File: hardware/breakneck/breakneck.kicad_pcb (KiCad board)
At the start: 2 copper layers, 53.3 x 64 mm, 82 parts, among them J1 CONN_EAST, J10 CONN_WEST, J2 GS2, J3 CONN_01X02, J4 GS3, J5 USB_C_Receptacle, J6 GS3, J7 CONN_OLED, J8 CONN_SOUTH, J9 CONN_JTAG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

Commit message: Flush connections from first batch of design rule check results.
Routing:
- net GND: track 43.6 -> 128.6 mm, vias 3 -> 16
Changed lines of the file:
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@@
   (general
     (links 242)
-    (no_connects 108)
-    (area 99.924999 63.924999 153.415001 128.075001)
+    (no_connects 94)
+    (area 87.650001 56.8 244.600001 146.625)
     (thickness 1.6)
     (drawings 59)
-    (tracks 478)
+    (tracks 541)
     (zones 0)
     (modules 82)
@@
   (segment (start 134.95 108.2) (end 137.1 108.2) (width 0.1524) (layer F.Cu) (net 1))
   (segment (start 133.5 106.75) (end 134.95 108.2) (width 0.1524) (layer F.Cu) (net 1))
+  (segment (start 121.4 112) (end 121.4 111.4) (width 0.1524) (layer F.Cu) (net 2))
+  (segment (start 121.4 111.4) (end 121 111) (width 0.1524) (layer F.Cu) (net 2))
+  (via (at 121 111) (size 0.6858) (drill 0.3302) (layers F.Cu B.Cu) (net 2))
+  (segment (start 121.4 112) (end 121.4 113.84) (width 0.1524) (layer F.Cu) (net 2))
+  (segment (start 121.4 113.84) (end 125.4 117.84) (width 0.1524) (layer F.Cu) (net 2))
+  (segment (start 125.4 117.84) (end 126.56 117.84) (width 0.1524) (layer F.Cu) (net 2))
+  (segment (start 126.56 117.84) (end 130 114.4) (width 0.1524) (layer F.Cu) (net 2))
+  (segment (start 132 116.5) (end 132 116.4) (width 0.1524) (layer F.Cu) (net 2))
+  (segment (start 132 116.4) (end 130 114.4) (width 0.1524) (layer F.Cu) (net 2))
+  (segment (start 142.2 103.9) (end 148.07 103.9) (width 0.1524) (layer F.Cu) (net 2))
+  (via (at 142.2 103.9) (size 0.6858) (drill 0.3302) (layers F.Cu B.Cu) (net 2))
+  (segment (start 140.11 103.9) (end 142.2 103.9) (width 0.1524) (layer B.Cu) (net 2))
+  (segment (start 148.065 103.895) (end 148.07 103.9) (width 0.1524) (layer F.Cu) (net 2))
+  (via (at 148.07 103.9) (size 0.6858) (drill 0.3302) (layers F.Cu B.Cu) (net 2))
+  (segment (start 148.065 103.895) (end 148.07 102.75) (width 0.1524) (layer F.Cu) (net 2) (status 20))
+  (segment (start 145.7 103.14) (end 147.68 103.14) (width 0.1524) (layer F.Cu) (net 2) (status 20))
+  (segment (start 140.11 103.9) (end 140.11 102.61) (width 0.1524) (layer B.Cu) (net 2))
+  (via (at 136 100) (size 0.6858) (drill 0.3302) (layers F.Cu B.Cu) (net 2))
+  (segment (start 136 101.5) (end 136 100) (width 0.1524) (layer F.Cu) (net 2))
+  (segment (start 140.11 103.9) (end 140.11 102.75) (width 0.1524) (layer F.Cu) (net 2) (status 20))
+  (via (at 140.11 103.9) (size 0.6858) (drill 0.3302) (layers F.Cu B.Cu) (net 2))
+  (segment (start 137.5 100) (end 136 100) (width 0.1524) (layer B.Cu) (net 2))
+  (segment (start 140.11 102.61) (end 137.5 100) (width 0.1524) (layer B.Cu) (net 2))
+  (segment (start 137.7 106.25) (end 137.7 107.2) (width 0.1524) (layer F.Cu) (net 2))
+  (via (at 142.25 109) (size 0.6858) (drill 0.3302) (layers F.Cu B.Cu) (net 2))
+  (segment (start 140.75 109) (end 142.25 109) (width 0.1524) (layer B.Cu) (net 2))
+  (via (at 140.75 109) (size 0.6858) (drill 0.3302) (layers F.Cu B.Cu) (net 2))
+  (segment (start 139.5 109) (end 140.75 109) (width 0.1524) (layer F.Cu) (net 2))
+  (segment (start 137.7 107.2) (end 139.5 109) (width 0.1524) (layer F.Cu) (net 2))
+  (segment (start 135.3 110.25) (end 135.3 110.2) (width 0.1524) (layer F.Cu) (net 2))
+  (segment (start 135.3 110.2) (end 136.5 109) (width 0.1524) (layer F.Cu) (net 2))
+  (segment (start 136.5 107.5) (end 137.7 106.3) (width 0.1524) (layer F.Cu) (net 2))
+  (via (at 136.5 107.5) (size 0.6858) (drill 0.3302) (layers F.Cu B.Cu) (net 2))
+  (segment (start 136.5 109) (end 136.5 107.5) (width 0.1524) (layer B.Cu) (net 2))
+  (via (at 136.5 109) (size 0.6858) (drill 0.3302) (layers F.Cu B.Cu) (net 2))
+  (segment (start 137.7 106.3) (end 137.7 106.25) (width 0.1524) (layer F.Cu) (net 2))
+  (segment (start 135.5 112.5) (end 135.5 110.45) (width 0.1524) (layer F.Cu) (net 2))
+  (segment (start 135.5 110.45) (end 135.3 110.25) (width 0.1524) (layer F.Cu) (net 2))
+  (segment (start 137.5 104) (end 137.5 106.05) (width 0.1524) (layer F.Cu) (net 2))
+  (segment (start 137.5 106.05) (end 137.7 106.25) (width 0.1524) (layer F.Cu) (net 2))
+  (segment (start 147.68 103.14) (end 148.07 102.75) (width 0.1524) (layer F.Cu) (net 2) (status 30))
+  (segment (start 140.2 118.88) (end 139.28 118.88) (width 0.1524) (layer F.Cu) (net 2))
+  (segment (start 139.28 118.88) (end 139.07 119.09) (width 0.1524) (layer F.Cu) (net 2))
+  (segment (start 132.42 112.5) (end 132.42 111.25) (width 0.1524) (layer F.Cu) (net 2))
+  (via (at 132.42 111.25) (size 0.6858) (drill 0.3302) (layers F.Cu B.Cu) (net 2))
+  (segment (start 129.92 110.7) (end 129.92 111.5) (width 0.1524) (layer F.Cu) (net 2))
+  (via (at 128.9 112) (size 0.6858) (drill 0.3302) (layers F.Cu B.Cu) (net 2))
+  (segment (start 129.42 112) (end 128.9 112) (width 0.1524) (layer F.Cu) (net 2))
+  (segment (start 129.92 111.5) (end 129.42 112) (width 0.1524) (layer F.Cu) (net 2))
+  (segment (start 132.5 97) (end 131.25 98.25) (width 0.1524) (layer F.Cu) (net 2))
+  (segment (start 129.92 98.58) (end 129.92 99.3) (width 0.1524) (layer F.Cu) (net 2))
+  (segment (start 130.25 98.25) (end 129.92 98.58) (width 0.1524) (layer F.Cu) (net 2))
+  (segment (start 131.25 98.25) (end 130.25 98.25) (width 0.1524) (layer F.Cu) (net 2))
+  (segment (start 132.37 103.25) (end 134.25 103.25) (width 0.1524) (layer F.Cu) (net 2))
+  (segment (start 134.25 103.25) (end 136 101.5) (width 0.1524) (layer F.Cu) (net 2))
+  (segment (start 103.5 123) (end 103.5 124.5) (width 0.1524) (layer F.Cu) (net 2))
+  (segment (start 103.5 124.5) (end 102.54 125.46) (width 0.1524) (layer F.Cu) (net 2))
+  (segment (start 110.25 94.075) (end 106.5 94.075) (width 0.1524) (layer F.Cu) (net 2))
+  (via (at 106.5 94.075) (size 0.6858) (drill 0.3302) (layers F.Cu B.Cu) (net 2))
+  (segment (start 110.25 89.075) (end 109.5 89.075) (width 0.1524) (layer F.Cu) (net 2))
+  (via (at 109.5 89.075) (size 0.6858) (drill 0.3302) (layers F.Cu B.Cu) (net 2))
+  (segment (start 145.72 67.04) (end 140.78 67.04) (width 0.1524) (layer B.Cu) (net 2))
+  (segment (start 140.78 67.04) (end 136.82 71) (width 0.1524) (layer B.Cu) (net 2))
   (segment (start 145.7 118.88) (end 145.7 120) (width 0.1524) (layer F.Cu) (net 2))
   (via (at 145.7 120) (size 0.6858) (drill 0.3302) (layers F.Cu B.Cu) (net 2))
@@
   (segment (start 145 97.48) (end 145 100) (width 0.1524) (layer F.Cu) (net 15))
   (via (at 144 106) (size 0.6858) (drill 0.3302) (layers F.Cu B.Cu) (net 15))
-  (segment (start 144 104) (end 144 106) (width 0.1524) (layer B.Cu) (net 15))
-  (via (at 144 104) (size 0.6858) (drill 0.3302) (layers F.Cu B.Cu) (net 15))
-  (segment (start 144 101) (end 144 104) (width 0.1524) (layer F.Cu) (net 15))
+  (segment (start 144 103) (end 144 106) (width 0.1524) (layer B.Cu) (net 15))
+  (via (at 144 103) (size 0.6858) (drill 0.3302) (layers F.Cu B.Cu) (net 15))
+  (segment (start 144 101) (end 144 103) (width 0.1524) (layer F.Cu) (net 15))
   (segment (start 145 100) (end 144 101) (width 0.1524) (layer F.Cu) (net 15))
   (segment (start 144.05 110.85) (end 144.05 106.05) (width 0.1524) (layer F.Cu) (net 15))
@@
   (segment (start 127.92 112.51) (end 127.93 112.5) (width 0.1524) (layer B.Cu) (net 82))
   (via (at 127.92 112.51) (size 0.6858) (drill 0.3302) (layers F.Cu B.Cu) (net 82))
-  (segment (start 140.11 107.25) (end 140 107.25) (width 0.1524) (layer F.Cu) (net 83))
-  (segment (start 140 107.25) (end 138.75 106) (width 0.1524) (layer F.Cu) (net 83))
+  (segment (start 140.11 107.25) (end 140 107.25) (width 0.1524) (layer F.Cu) (net 83) (status 30))
+  (segment (start 140 107.25) (end 138.75 106) (width 0.1524) (layer F.Cu) (net 83) (status 10))
   (segment (start 138.75 106) (end 138.75 102.45) (width 0.1524) (layer F.Cu) (net 83))
   (segment (start 138.75 102.45) (end 138.4 102.1) (width 0.1524) (layer F.Cu) (net 83))

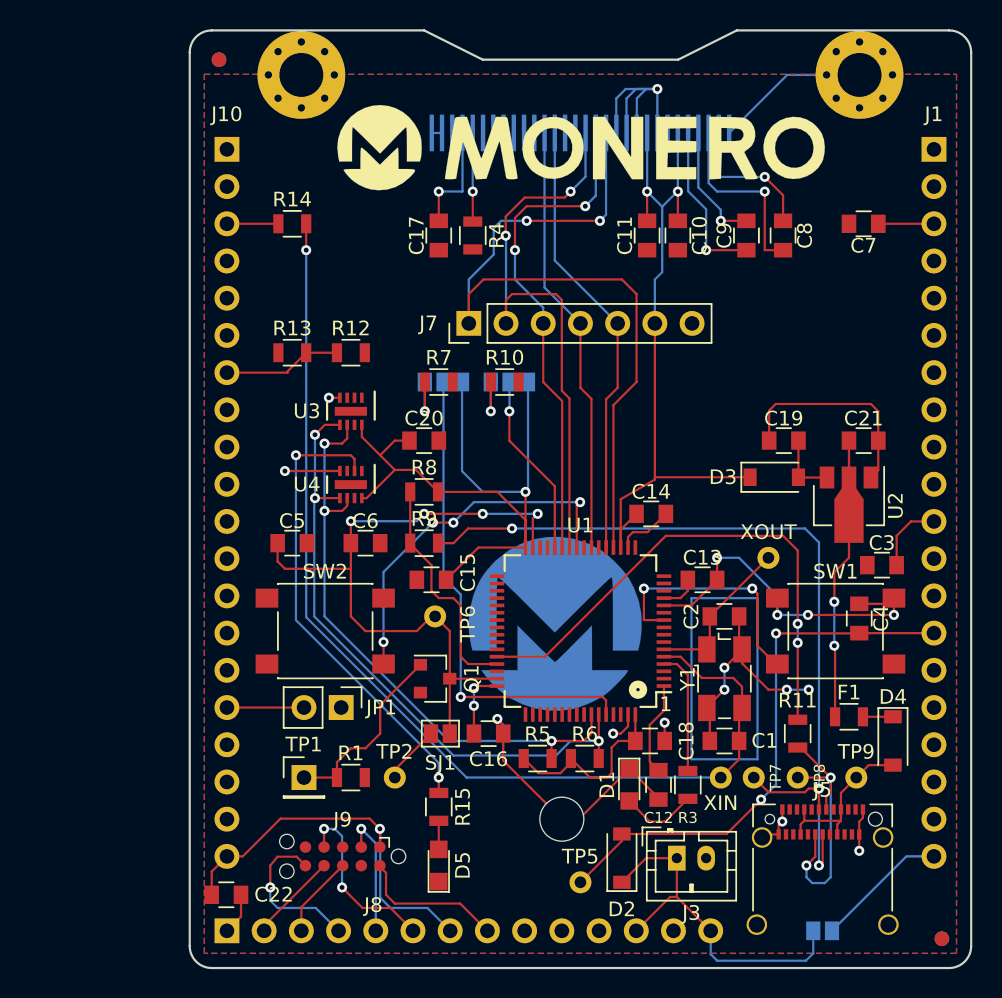
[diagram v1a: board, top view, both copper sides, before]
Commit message: Corrected scaling and rotation of shapes, and connected ground paths.
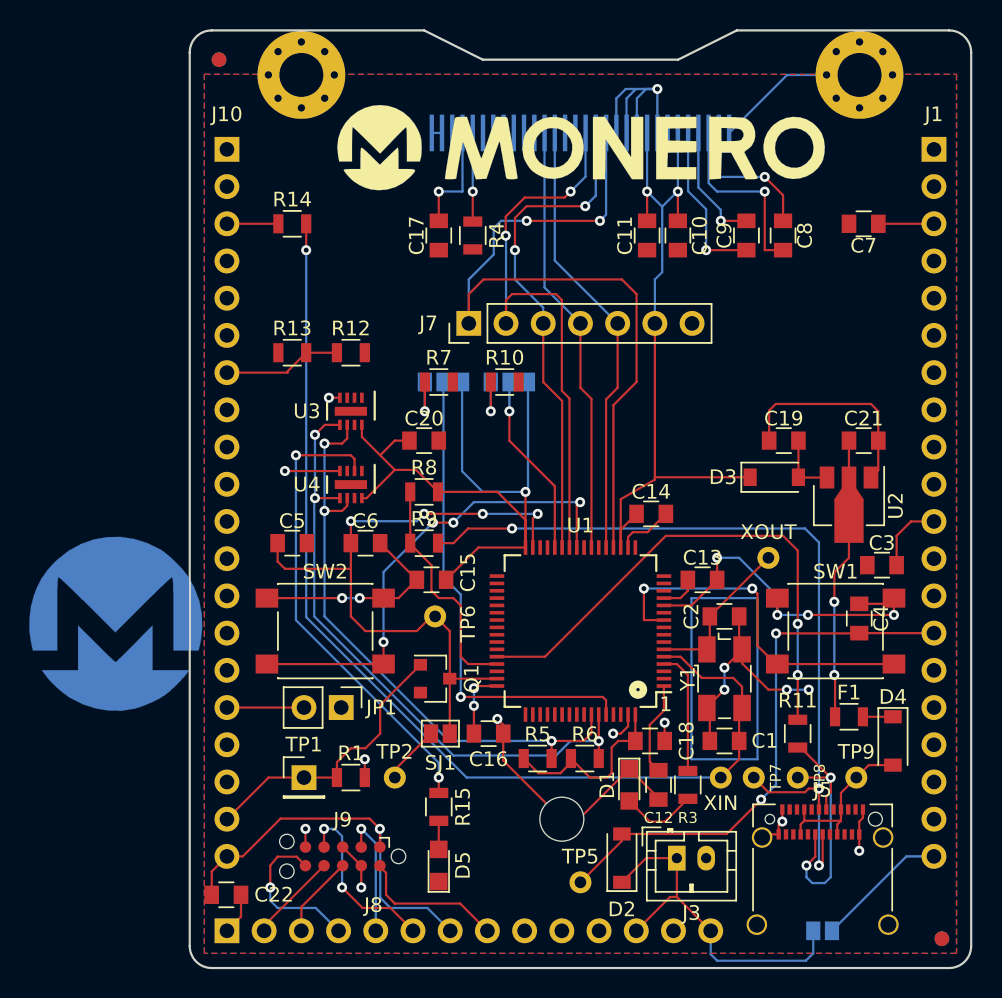
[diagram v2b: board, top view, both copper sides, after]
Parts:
- moved LOGO1 30.0 mm to (95.0, 104.5)
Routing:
- net GND: track 128.6 -> 148.6 mm, vias 16 -> 21
- net Net-(SW2-Pad2): track 24.9 -> 32.9 mm
- net Net-(SW1-Pad2): track 16.8 -> 24.8 mm
- net /GLITCH: track 13.0 -> 19.4 mm
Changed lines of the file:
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@@
   (general
     (links 242)
-    (no_connects 94)
-    (area 87.650001 56.8 244.600001 146.625)
+    (no_connects 87)
+    (area 99.924999 63.924999 153.415001 128.075001)
     (thickness 1.6)
     (drawings 59)
-    (tracks 541)
+    (tracks 560)
     (zones 0)
     (modules 82)
@@
   )
   (module Monero_Logos:MoneroCircleCombi (layer B.Cu)
-    (at 125 104.5 180)
+    (at 95 104.5 180)
     (fp_text reference LOGO1 (at 0 0 180) (layer B.SilkS) hide
       (effects (font (thickness 0.3)) (justify mirror))
@@
       (at (xyz 0 0 0))
       (scale (xyz 1 1 1))
-      (rotate (xyz 0 0 90))
+      (rotate (xyz 0 0 0))
     )
   )
@@
     (model ${KIPRJMOD}/modules/packages3d/TO_SOT_Packages_SMD.3dshapes/SOT-89-3.wrl
       (at (xyz 0.02 0 0))
-      (scale (xyz 0.39 0.39 0.39))
-      (rotate (xyz 0 0 90))
+      (scale (xyz 1 1 1))
+      (rotate (xyz 0 0 0))
     )
   )
@@
   (segment (start 134.95 108.2) (end 137.1 108.2) (width 0.1524) (layer F.Cu) (net 1))
   (segment (start 133.5 106.75) (end 134.95 108.2) (width 0.1524) (layer F.Cu) (net 1))
+  (segment (start 113.23 102.75) (end 111.6 102.75) (width 0.1524) (layer F.Cu) (net 2))
+  (segment (start 110.4 102.75) (end 105.27 102.75) (width 0.1524) (layer F.Cu) (net 2))
+  (via (at 110.4 102.75) (size 0.6858) (drill 0.3302) (layers F.Cu B.Cu) (net 2))
+  (segment (start 111.6 102.75) (end 110.4 102.75) (width 0.1524) (layer B.Cu) (net 2))
+  (via (at 111.6 102.75) (size 0.6858) (drill 0.3302) (layers F.Cu B.Cu) (net 2))
+  (segment (start 113.23 102.75) (end 114.25 102.75) (width 0.1524) (layer F.Cu) (net 2))
+  (segment (start 114.25 102.75) (end 115.5 101.5) (width 0.1524) (layer F.Cu) (net 2))
+  (segment (start 113 99) (end 115.5 101.5) (width 0.1524) (layer F.Cu) (net 2))
+  (segment (start 111.95 115) (end 111.95 113.75) (width 0.1524) (layer F.Cu) (net 2))
+  (via (at 111.95 113.75) (size 0.6858) (drill 0.3302) (layers F.Cu B.Cu) (net 2))
+  (segment (start 111.71 121.015) (end 111.71 122.5) (width 0.1524) (layer F.Cu) (net 2))
+  (via (at 111.71 122.5) (size 0.6858) (drill 0.3302) (layers F.Cu B.Cu) (net 2))
+  (segment (start 107.9 119.745) (end 107.9 118.5) (width 0.1524) (layer F.Cu) (net 2))
+  (via (at 107.9 118.5) (size 0.6858) (drill 0.3302) (layers F.Cu B.Cu) (net 2))
+  (segment (start 110.44 119.745) (end 111.71 121.015) (width 0.1524) (layer F.Cu) (net 2))
   (segment (start 121.4 112) (end 121.4 111.4) (width 0.1524) (layer F.Cu) (net 2))
   (segment (start 121.4 111.4) (end 121 111) (width 0.1524) (layer F.Cu) (net 2))
@@
   (segment (start 145 94.52) (end 145 92) (width 0.1524) (layer F.Cu) (net 15))
   (segment (start 145 97.48) (end 145 100) (width 0.1524) (layer F.Cu) (net 15))
-  (via (at 144 106) (size 0.6858) (drill 0.3302) (layers F.Cu B.Cu) (net 15))
-  (segment (start 144 103) (end 144 106) (width 0.1524) (layer B.Cu) (net 15))
+  (via (at 144 108) (size 0.6858) (drill 0.3302) (layers F.Cu B.Cu) (net 15))
+  (segment (start 144 103) (end 144 108) (width 0.1524) (layer B.Cu) (net 15))
   (via (at 144 103) (size 0.6858) (drill 0.3302) (layers F.Cu B.Cu) (net 15))
   (segment (start 144 101) (end 144 103) (width 0.1524) (layer F.Cu) (net 15))
   (segment (start 145 100) (end 144 101) (width 0.1524) (layer F.Cu) (net 15))
-  (segment (start 144.05 110.85) (end 144.05 106.05) (width 0.1524) (layer F.Cu) (net 15))
+  (segment (start 144.05 110.85) (end 144.05 108.05) (width 0.1524) (layer F.Cu) (net 15))
   (segment (start 130 116.6) (end 131.4 118) (width 0.1524) (layer F.Cu) (net 16))
   (segment (start 132.45 118) (end 134 116.45) (width 0.1524) (layer F.Cu) (net 16))
@@
   (segment (start 107.95 86) (end 110.05 86) (width 0.1524) (layer F.Cu) (net 70))
   (segment (start 120.97 106.75) (end 124.25 106.75) (width 0.1524) (layer F.Cu) (net 72))
-  (segment (start 141.5 105.8) (end 141.5 111.05) (width 0.1524) (layer F.Cu) (net 72))
-  (via (at 141.5 105.8) (size 0.6858) (drill 0.3302) (layers F.Cu B.Cu) (net 72))
-  (segment (start 141.5 104.5) (end 141.5 105.8) (width 0.1524) (layer B.Cu) (net 72))
+  (segment (start 141.5 108) (end 141.5 111.05) (width 0.1524) (layer F.Cu) (net 72))
+  (via (at 141.5 108) (size 0.6858) (drill 0.3302) (layers F.Cu B.Cu) (net 72))
+  (segment (start 141.5 104.5) (end 141.5 108) (width 0.1524) (layer B.Cu) (net 72))
   (via (at 141.5 104.5) (size 0.6858) (drill 0.3302) (layers F.Cu B.Cu) (net 72))
   (segment (start 141.5 99.5) (end 141.5 104.5) (width 0.1524) (layer F.Cu) (net 72))
@@
   (segment (start 115.05 99) (end 115.05 99.05) (width 0.1524) (layer F.Cu) (net 73))
   (segment (start 115.05 99) (end 115.05 95.5) (width 0.1524) (layer F.Cu) (net 73) (status 10))
+  (segment (start 107.8 115) (end 105.38 115) (width 0.1524) (layer F.Cu) (net 79))
+  (segment (start 105.38 115) (end 102.54 117.84) (width 0.1524) (layer F.Cu) (net 79))
   (segment (start 110.05 115) (end 110.05 113.95) (width 0.1524) (layer F.Cu) (net 79))
   (segment (start 113 110.05) (end 115.75 107.3) (width 0.1524) (layer F.Cu) (net 79))
@@
   (segment (start 127.92 112.51) (end 127.93 112.5) (width 0.1524) (layer B.Cu) (net 82))
   (via (at 127.92 112.51) (size 0.6858) (drill 0.3302) (layers F.Cu B.Cu) (net 82))
+  (segment (start 140.11 107.25) (end 148.07 107.25) (width 0.1524) (layer F.Cu) (net 83))
   (segment (start 140.11 107.25) (end 140 107.25) (width 0.1524) (layer F.Cu) (net 83) (status 30))
   (segment (start 140 107.25) (end 138.75 106) (width 0.1524) (layer F.Cu) (net 83) (status 10))
@@
   (segment (start 131 102.1) (end 131 104.25) (width 0.1524) (layer F.Cu) (net 83))
   (segment (start 131 104.25) (end 132.37 104.25) (width 0.1524) (layer F.Cu) (net 83))
+  (segment (start 105.27 107.25) (end 113.23 107.25) (width 0.1524) (layer F.Cu) (net 84))
   (segment (start 116.6 97.6) (end 113.23 100.97) (width 0.1524) (layer B.Cu) (net 84))
   (via (at 116.6 97.6) (size 0.6858) (drill 0.3302) (layers F.Cu B.Cu) (net 84))

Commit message: Connected UART and JTAG, improved padded hole, and moved premature logo.
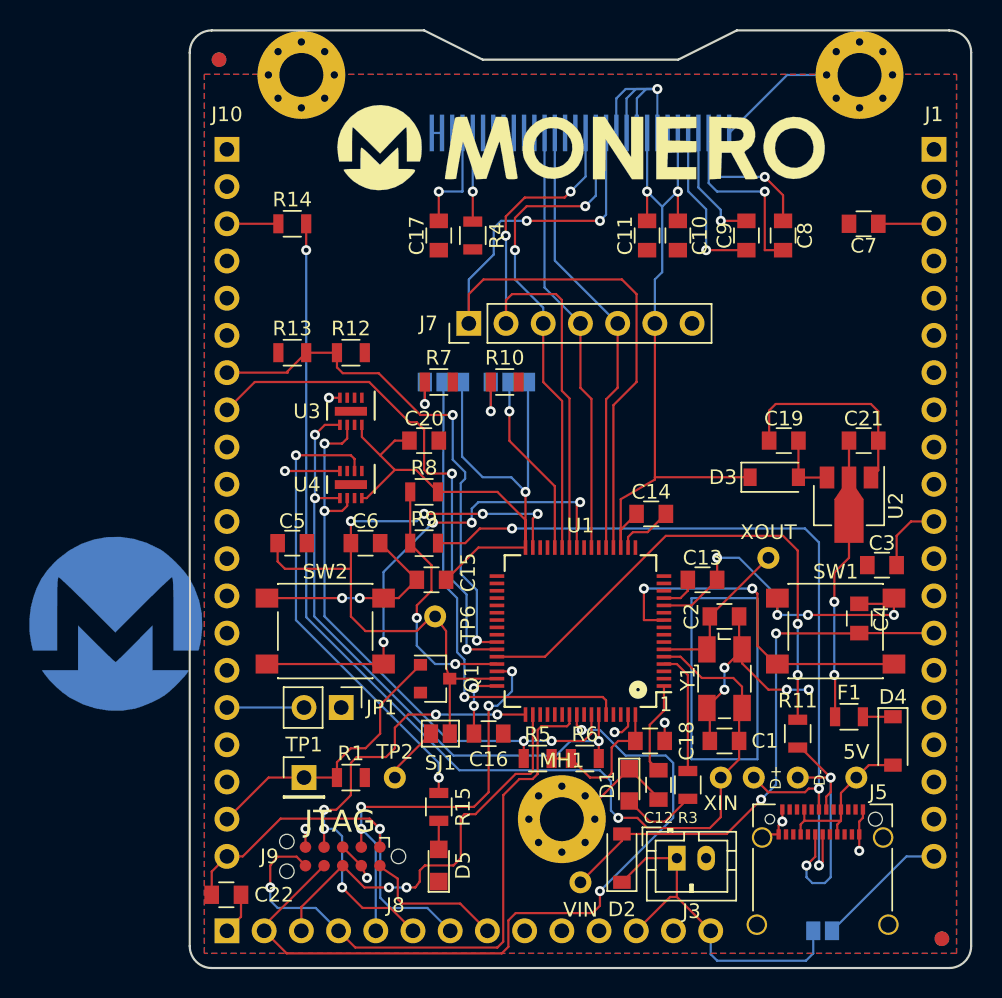
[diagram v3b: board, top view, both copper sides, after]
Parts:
- MH1: footprint Mounting_Holes:MountingHole_3mm -> Mounting_Holes:MountingHole_3mm_Pad_Via
- turned R5 to 180 degrees
- renumbered TP9 to 5V, TP7 to D+, TP8 to D-, TP5 to VIN
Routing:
- net /JTAG_TRST: track 6.14 -> 52.3 mm, vias 0 -> 2
- net /UART_RX: track 0.00 -> 34.8 mm, vias 0 -> 2
- net /JTAG_TDO: track 10.9 -> 41.7 mm
- net /UART_TX: track 8.13 -> 36.1 mm, vias 0 -> 2
- net /JTAG_TDI: track 5.61 -> 28.5 mm, vias 0 -> 2
- net /JTAG_TMS: track 8.62 -> 29.5 mm, vias 1 -> 4
- net /JTAG_TCK: track 12.3 -> 32.1 mm, vias 2 -> 5
- net GND: track 148.6 -> 138.0 mm, vias 21 -> 19
- net /OSC_IN: track 72.7 -> 78.3 mm, vias 1 -> 2
- net +3V3: track 177.0 -> 173.8 mm
- net /USB_P: track 15.9 -> 17.5 mm, vias 0 -> 2
- net Net-(J4-Pad1): track 4.00 -> 3.00 mm
- net Net-(SW2-Pad2): track 32.9 -> 33.4 mm
- net /I2C_SCL: vias 3 -> 4
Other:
- board text added: "JTAG"
